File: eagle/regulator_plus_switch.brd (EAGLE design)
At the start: 184.7 x 181.9 mm, 60 parts, among them IC1 LT1352PA, IC2 LT1352PA, IC3 DG419DJN, IC4 LT1352PA, T1 2N3904, T2 2N3904

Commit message: pa 97 circuit
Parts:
- removed C5: 10n, rcl:C075-032X103
- removed D7: 1N4148DO35-10, diode:DO35-10
- removed DC1: (no value), dc-dc-converter:NCS
- removed IC1: LT1352PA, linear-technology:DIL08
- removed OK1: PC817, optocoupler:DIL04
- removed Q1, Q2: (no value), transistor-power:TO220BV
- removed R1, R2: 65, rcl:0207/10
- removed R10, R11, R9: 10k, rcl:0207/10
- removed R12: 250, rcl:0207/15
- removed R15, R5, R7: 1M, resistor:0414/15
- removed R3, R4: 100, rcl:0207/10
- removed R6: 100k, rcl:0207/10
- removed R8: 50k, rcl:0207/10
- removed T1, T2: 2N3904, transistor:TO92
- added U$3: PA97, apex:7SIP
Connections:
- removed net N$11: Q2.G, R4.1
- removed net N$12: OK1.3, R4.2, R6.2, T2.1
- removed net N$14: Q2.S, R2.2, T2.2
- removed net N$16: DC1.P$6, OK1.4
- removed net N$17: C5.1, R9.1
- removed net N$18: IC1.2, R10.1, R9.2
- removed net N$19: C5.2, IC1.1, R12.2
- removed net N$20: IC1.3, R11.1
- removed net N$21: R11.2, R7.1, R8.2
- removed net N$22: OK1.1, R12.1
- removed net N$23: R15.1, R7.2
- removed net N$6: Q1.G, R3.1
- removed net N$7: D7.C, Q2.D, R3.2, R5.1, T1.1
- removed net N$8: Q1.S, R1.2, T1.2
- net +15V: no longer DC1.P$8, DC1.P$9, IC1.8
- net -15V: no longer IC1.4
- net GND: no longer DC1.P$2, DC1.P$3, OK1.2, R8.1
- net N$10: no longer D7.A, R1.1, R15.2, T1.3
- net N$28: no longer R10.2
- net V+: now also U$3.P$7; no longer Q1.D, R5.2
- net V-: now also U$3.P$6; no longer DC1.P$7, R2.1, R6.1, T2.3
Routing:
- net V-: track 139.7 -> 56.1 mm
- net N$7: track 76.3 -> 0.00 mm
- net N$19: track 68.7 -> 0.00 mm
- net N$21: track 54.6 -> 0.00 mm
- net V+: track 99.5 -> 47.8 mm
- net N$18: track 42.0 -> 0.00 mm
- net N$14: track 41.6 -> 0.00 mm, vias 2 -> 0
- net N$10: track 115.7 -> 74.5 mm
- net N$8: track 40.2 -> 0.00 mm, vias 2 -> 0
- net N$12: track 34.6 -> 0.00 mm
- net N$22: track 29.7 -> 0.00 mm
- net +15V: track 235.6 -> 216.3 mm
- net N$16: track 18.6 -> 0.00 mm
- net N$17: track 16.5 -> 0.00 mm
- net N$20: track 15.5 -> 0.00 mm
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
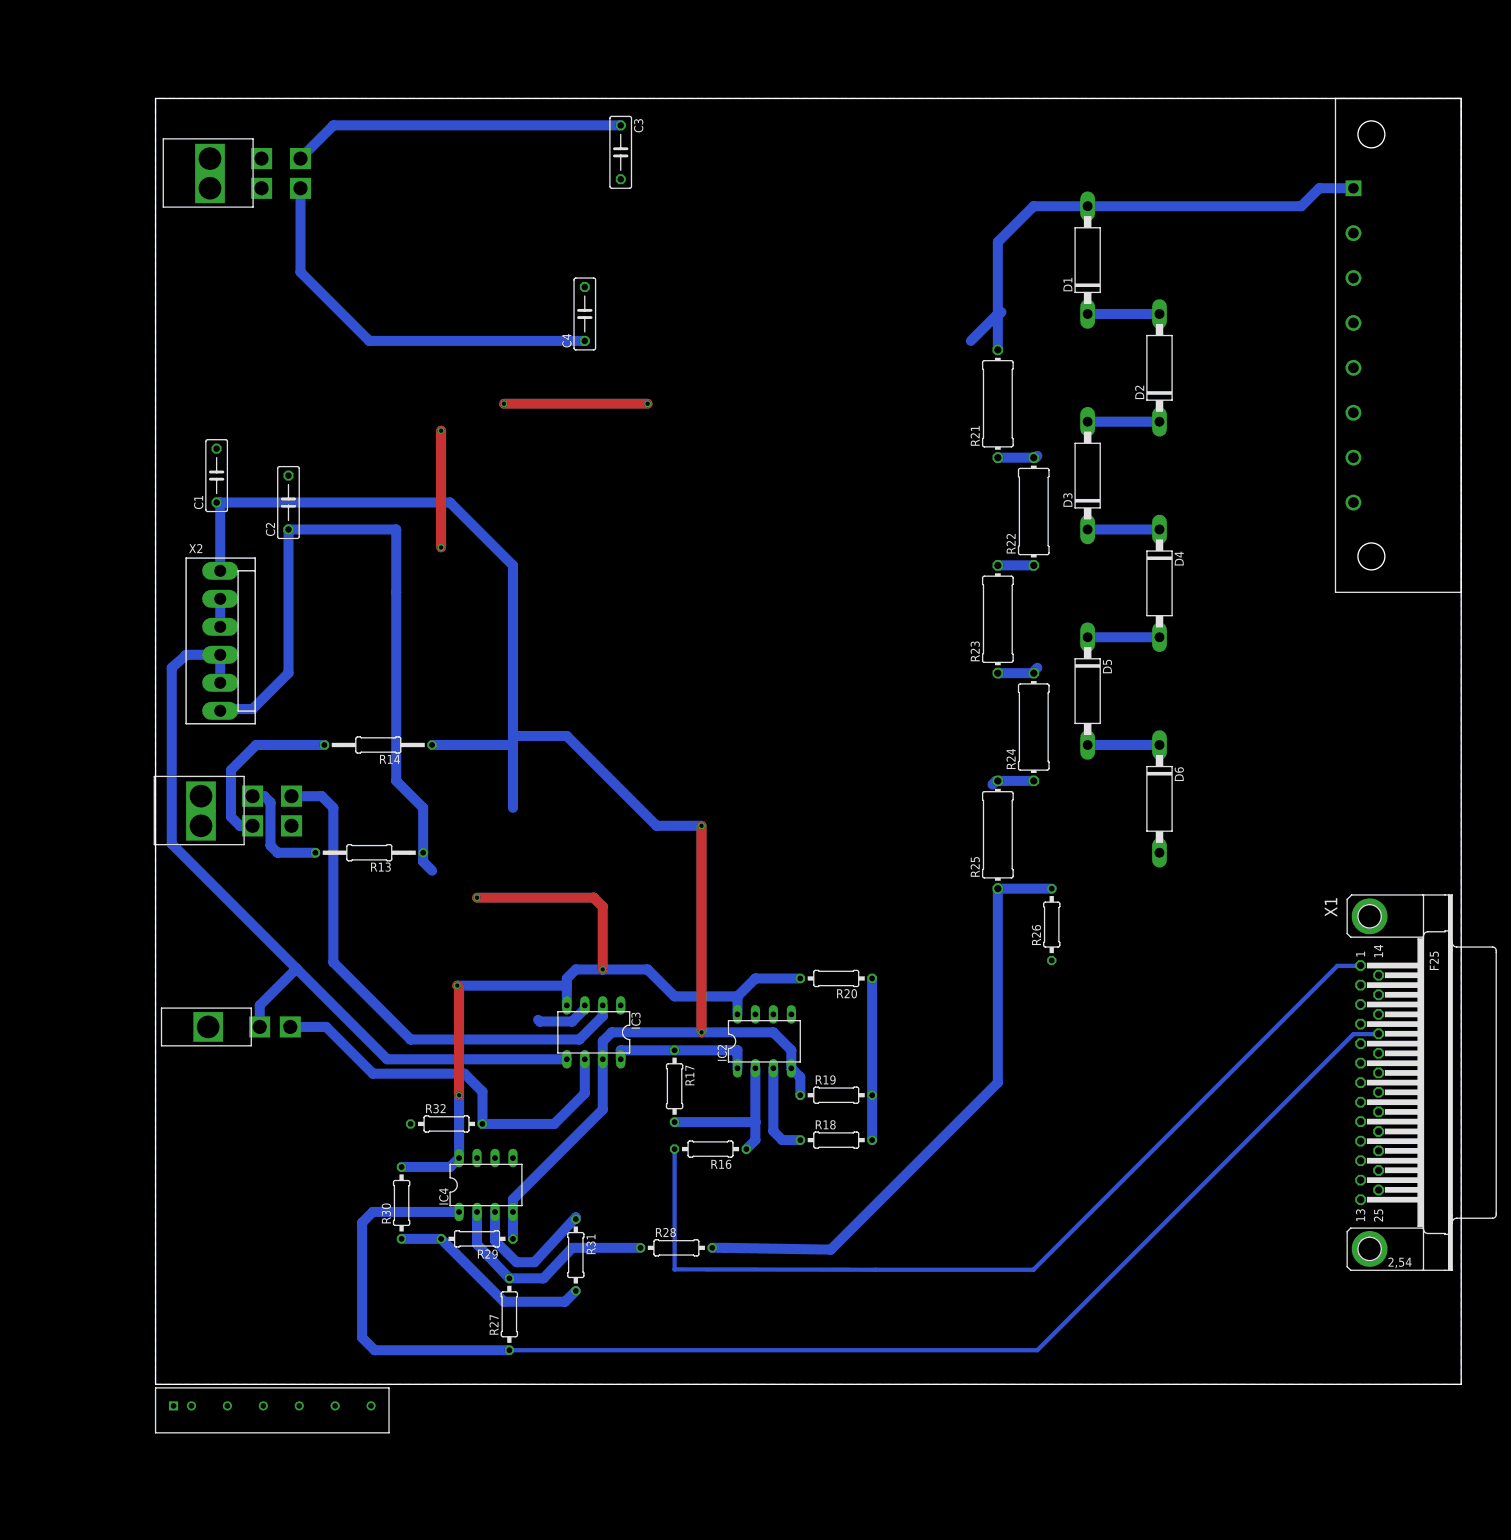
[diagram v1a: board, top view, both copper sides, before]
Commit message: add display out
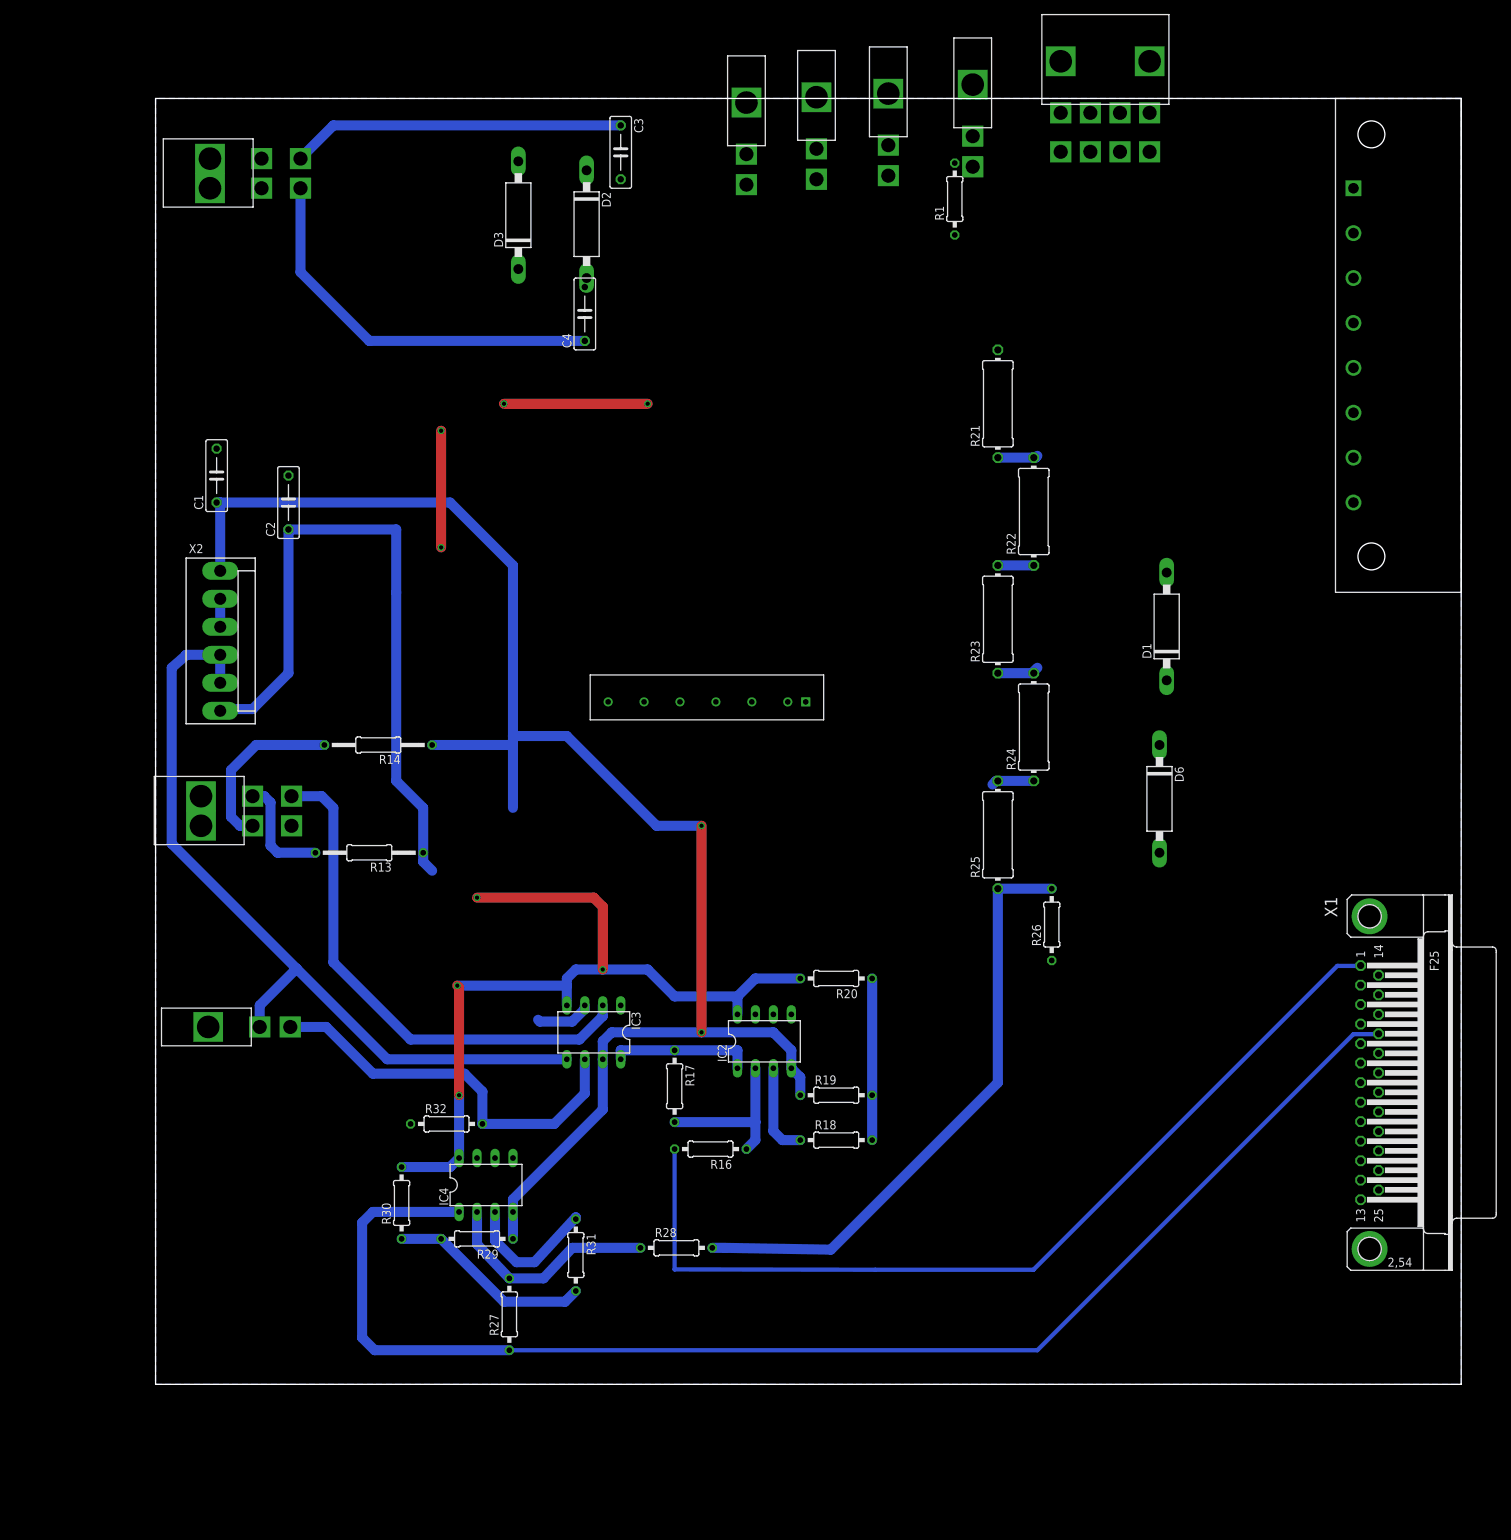
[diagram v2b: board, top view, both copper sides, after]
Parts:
- removed D4, D5: P6KEXX, diode:CB417-15
- added J17: 5669-8, con-molex:5669-8
- added J23, J24, J25, J26: 5569-2, con-molex:5569-2
- added R1: 220, rcl:0207/10
- D1, D2, D3, D6: value P6KEXX -> P6KEXXA; device diode:CB417-15 -> diode:C1702-15
- moved U$3 133.8 mm to (91.9, 96.5), turned to 180 degrees
- moved D3 88.5 mm to (51.3, 165.4)
- moved D2 83.5 mm to (61.0, 164.1), turned to 270 degrees
- moved D1 53.0 mm to (143.0, 107.2)
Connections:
- removed net N$2: D2.C, D3.A
- removed net N$3: D3.C, D4.C
- removed net N$4: D4.A, D5.C
- removed net N$5: D5.A, D6.C
- new net N$6: J23.P$1, J24.P$1
- new net N$7: J26.P$1, R1.2
- net +5V: now also J25.P$1, R1.1
- net GND: now also D2.A, D3.C, J23.P$2, J24.P$2, J25.P$2, J26.P$2
- net N$1: now also D6.C; no longer D2.A
- net N$34: now also J17.P$1
- net V+: now also D2.C
- net V-: now also D3.A
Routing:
- net N$10: track 74.5 -> 0.00 mm
- net N$5: track 10.2 -> 0.00 mm
- net N$4: track 10.2 -> 0.00 mm
- net N$3: track 10.2 -> 0.00 mm
- net N$2: track 10.2 -> 0.00 mm
- net N$1: track 10.2 -> 0.00 mm

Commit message: Test layouts pa97
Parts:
- removed D1, D6: P6KEXXA, diode:C1702-15
- removed J17: 5669-8, con-molex:5669-8
- removed J23, J24, J25, J26: 5569-2, con-molex:5569-2
- removed U$1, U$2: 5569-4, con-molex:5669-4
- removed U$3: PA97, apex:7SIP
- removed U$5: 640584-1, con-amp-te:640584-1
- removed X1: (no value), con-subd:F25HP
- removed X2: (no value), con-molex:KK-156-6
- added C5, C7: 10p, rcl:C075-032X103
- added C6: 10n, rcl:C075-032X103
- added D10, D9: 1n4742, diode:DO41Z10
- added D7, D8: P6KEXXA, diode:C1702-15
- added DISPLAY: 5669-8, con-molex:5669-8
- added DISPLAYPOWER, GROUND, LED, MAN/EXT, UNK: 5569-2, con-molex:5569-2
- added EXTERNAL: (no value), con-subd:F25HP
- added HVIN, POT1: 5569-4, con-molex:5669-4
- added KK1: SK125/50C247, heatsink:C247-050
- added OUT: 640584-1, con-amp-te:640584-1
- added POWER: (no value), con-molex:KK-156-6
- added R2, R3, R4: 1M, rcl:0207/10
- added R5, R6, R7: 25.5k, rcl:0207/10
- R21, R22, R23, R24, R25: device resistor:0414/15 -> resistor:0207/10
- R26: value 50k -> 5k
- R32: device rcl:0207/10 -> rcl:0207/15
- U$4: value 5569-2 -> PA97; device con-molex:5569-2 -> apex:7SIP
- moved C3 74.5 mm to (19.8, 115.6), turned to 90 degrees
- moved D3 73.9 mm to (27.2, 95.5), turned to 180 degrees
- moved C4 71.4 mm to (23.6, 90.4), turned to 0 degrees
- moved C2 66.9 mm to (27.9, 58.4), turned to 0 degrees
- moved U$4 65.6 mm to (62.0, 96.0), turned to 0 degrees
- moved R14 63.3 mm to (23.1, 27.7)
- moved D2 54.8 mm to (29.2, 119.4), turned to 90 degrees
- moved C1 54.2 mm to (29.0, 78.2), turned to 0 degrees
- moved R21 50.0 mm to (118.9, 88.6)
- moved R22 45.0 mm to (126.2, 78.5)
- moved R23 39.9 mm to (119.1, 68.3)
- moved R1 37.8 mm to (91.7, 136.4)
- moved R24 34.9 mm to (126.5, 58.2)
- moved R13 33.1 mm to (25.7, 42.4), turned to 135 degrees
- moved R25 29.7 mm to (119.4, 48.0)
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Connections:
- removed net N$1: D1.C, D6.C
- removed net N$10: D1.A, R21.2, U$5.P$1
- new net N$11: C7.2, D8.A, OUT.P$1, R21.2, R3.2, U$4.P$5
- new net N$12: R2.1, R4.2
- new net N$14: R5.1, R6.2
- new net N$16: R6.1, R7.1
- new net N$18: R2.2, R3.1
- new net N$29: D10.C, D9.C
- new net N$3: C5.1, U$4.P$3
- new net N$38: C7.1, D10.A, R4.1, R5.2, U$4.P$1
- new net N$4: C5.2, U$4.P$4
- new net N$8: D7.C, D8.C
- net +15V: now also POWER.6; no longer X2.6
- net +5V: now also C6.1, DISPLAYPOWER.P$1, MAN/EXT.P$1, POWER.4, POWER.5; no longer J25.P$1, U$4.P$1, X2.4, X2.5
- net -15V: now also POWER.1; no longer X2.1
- net CMD1: now also EXTERNAL.1; no longer X1.1
- net GND: now also C6.2, D7.A, DISPLAYPOWER.P$2, EXTERNAL.10, EXTERNAL.12, EXTERNAL.14, EXTERNAL.16, EXTERNAL.2, EXTERNAL.25, EXTERNAL.4, EXTERNAL.6, EXTERNAL.8, GROUND.P$2, HVIN.P$1, HVIN.P$2, LED.P$2, POWER.2, POWER.3, R7.2, UNK.P$2; no longer D6.A, J23.P$2, J24.P$2, J25.P$2, J26.P$2, U$2.P$1, U$2.P$2, X1.10, X1.12, X1.14, X1.16, X1.2, X1.25, X1.4, X1.6, X1.8, X2.2, X2.3
- net MAN: now also MAN/EXT.P$2; no longer U$4.P$2
- net N$13: now also POT1.P$4; no longer U$1.P$4
- net N$15: now also POT1.P$1; no longer U$1.P$1
- net N$28: now also D9.A, U$4.P$2
- net N$34: now also DISPLAY.P$1; no longer J17.P$1
- net N$35: now also EXTERNAL.17; no longer X1.17
- net N$6: now also GROUND.P$1, UNK.P$1; no longer J23.P$1, J24.P$1
- net N$7: now also LED.P$1; no longer J26.P$1
- net N$9: now also POT1.P$2; no longer U$1.P$2
- net V+: now also HVIN.P$4, U$4.P$7; no longer U$2.P$4, U$3.P$7
- net V-: now also HVIN.P$3, U$4.P$6; no longer U$2.P$3, U$3.P$6
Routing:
- net +5V: track 115.3 -> 297.2 mm
- net N$34: track 85.2 -> 255.4 mm
- net N$38: track 0.00 -> 149.7 mm
- net N$11: track 0.00 -> 132.4 mm
- net V+: track 47.8 -> 156.4 mm
- net +15V: track 216.3 -> 128.7 mm, vias 4 -> 2
- net V-: track 56.1 -> 130.3 mm
- net GND: track 48.7 -> 7.95 mm, vias 4 -> 0
- net N$35: track 212.7 -> 178.2 mm
- net N$3: track 0.00 -> 24.5 mm
- net CMD1: track 131.9 -> 110.4 mm
- net N$28: track 0.00 -> 20.8 mm
- net N$13: track 74.0 -> 54.2 mm
- net N$4: track 0.00 -> 19.2 mm
- net N$15: track 24.9 -> 8.60 mm
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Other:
- board size 184.7 x 181.9 mm -> 152.4 x 152.4 mm

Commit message: regulator
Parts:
- added C8, C9: cc, rcl:C075-032X103
- added Q1, Q2: 2N3906, transistor-pnp:TO92
- added R10, R12: rb, rcl:0207/10
- added R11, R8: rlim, rcl:0207/10
- added R15, R9: rl, rcl:0207/10
- added T1, T2: 2N3904, transistor:TO92
- moved OUT 49.5 mm to (136.9, 77.2)
- moved EXTERNAL 42.5 mm to (108.5, 11.7), turned to 180 degrees
- moved R22 18.9 mm to (124.7, 59.7), turned to 180 degrees
- moved R21 18.3 mm to (119.6, 70.4)
- moved R23 14.8 mm to (124.7, 54.6), turned to 0 degrees
- moved R24 8.82 mm to (124.7, 49.5), turned to 180 degrees
- moved R26 5.89 mm to (120.9, 38.6), turned to 180 degrees
- moved R25 4.34 mm to (120.9, 43.9), turned to 0 degrees
- moved D8 3.84 mm to (112.5, 85.6)
- moved D7 3.09 mm to (105.7, 70.4)
- moved C7 2.03 mm to (85.1, 111.8)
- moved DISPLAY 0.80 mm to (108.2, 142.5)
- moved D9 0.76 mm to (59.4, 116.1)
- moved D10 0.25 mm to (49.3, 112.0)
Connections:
- net N$28 renamed VIN+
- net N$38 renamed VIN-
- new net N$1: R11.2, R12.2, T2.3
- new net N$10: C8.2, Q1.2, Q2.1, R9.2
- new net N$17: C9.2, R12.1, T1.2
- new net N$19: C9.1, R15.1, T1.1, T2.2
- new net N$2: C8.1, Q2.2, R10.1
- new net N$5: Q1.3, R10.2, R8.1
- new net V+_SAFE: Q1.1, U$4.P$7
- new net V-_SAFE: T2.1, U$4.P$6
- net GND: now also R15.2, R9.1
- net V+: now also Q2.3, R8.2; no longer U$4.P$7
- net V-: now also R11.1, T1.3; no longer U$4.P$6
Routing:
- net GND: track 7.95 -> 243.0 mm, vias 0 -> 8
- net V-_SAFE: track 0.00 -> 79.4 mm
- net VIN+: track 20.8 -> 82.1 mm, vias 0 -> 1
- net N$35: track 178.2 -> 126.3 mm
- net CMD1: track 110.4 -> 67.9 mm
- net V+_SAFE: track 0.00 -> 36.2 mm, vias 0 -> 2
- net V-: track 130.3 -> 163.1 mm
- net N$10: track 0.00 -> 32.8 mm
- net N$19: track 0.00 -> 27.4 mm
- net V+: track 156.4 -> 138.5 mm
- net N$34: track 255.4 -> 238.8 mm
- net N$2: track 0.00 -> 14.3 mm
- net N$17: track 0.00 -> 14.0 mm
- net N$11: track 132.4 -> 119.7 mm
- net N$5: track 0.00 -> 7.37 mm
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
